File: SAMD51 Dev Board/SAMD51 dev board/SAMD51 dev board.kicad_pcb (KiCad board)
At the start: 4 copper layers, 98.9 x 130 mm, 56 parts, among them IC1 MCP1603-330I_MC, IC2 MCP1603-180I_MC, J1 Conn_02x08_Top_Bottom, J10 Conn_02x16_Top_Bottom, J11 Conn_01x07, J12 Conn_01x05, J13 Conn_01x08, J14 Conn_02x16_Top_Bottom, J15 Conn_01x05, J16 Conn_01x06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

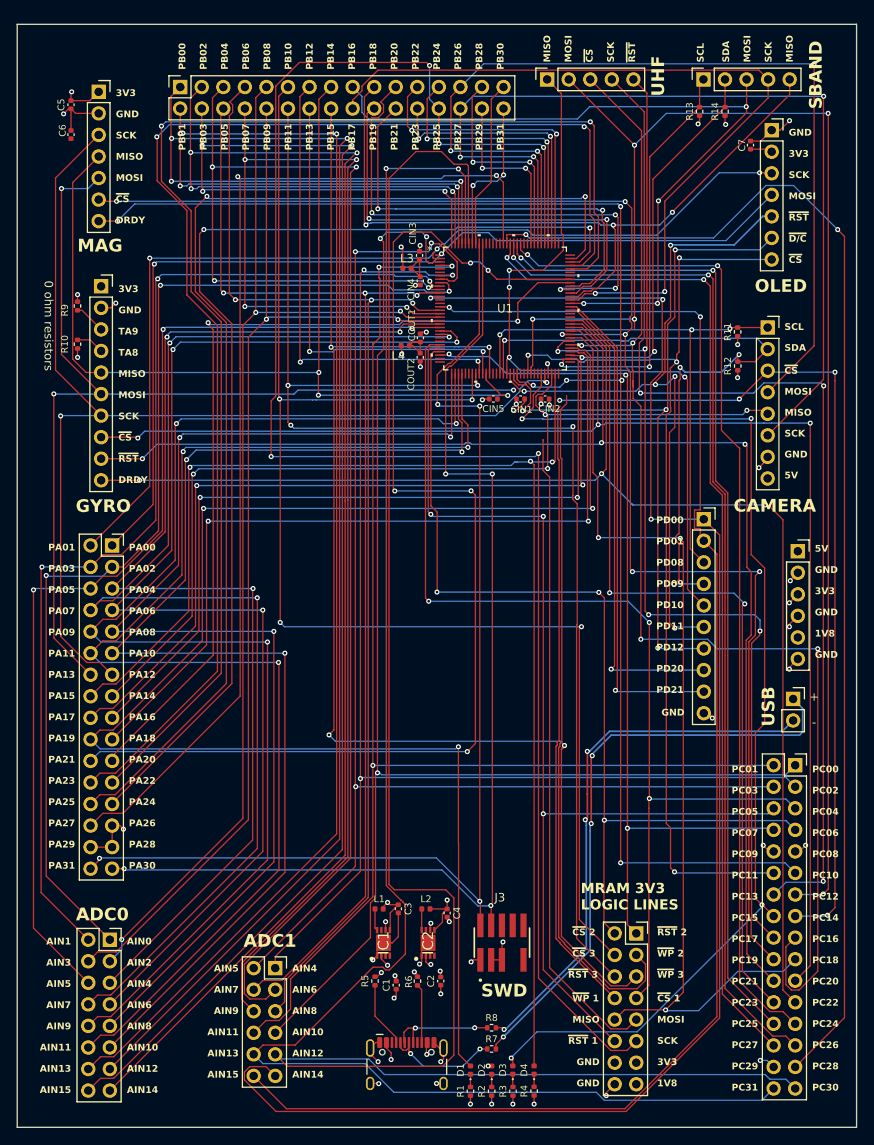
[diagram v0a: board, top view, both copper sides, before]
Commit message: routed samd51 breakout
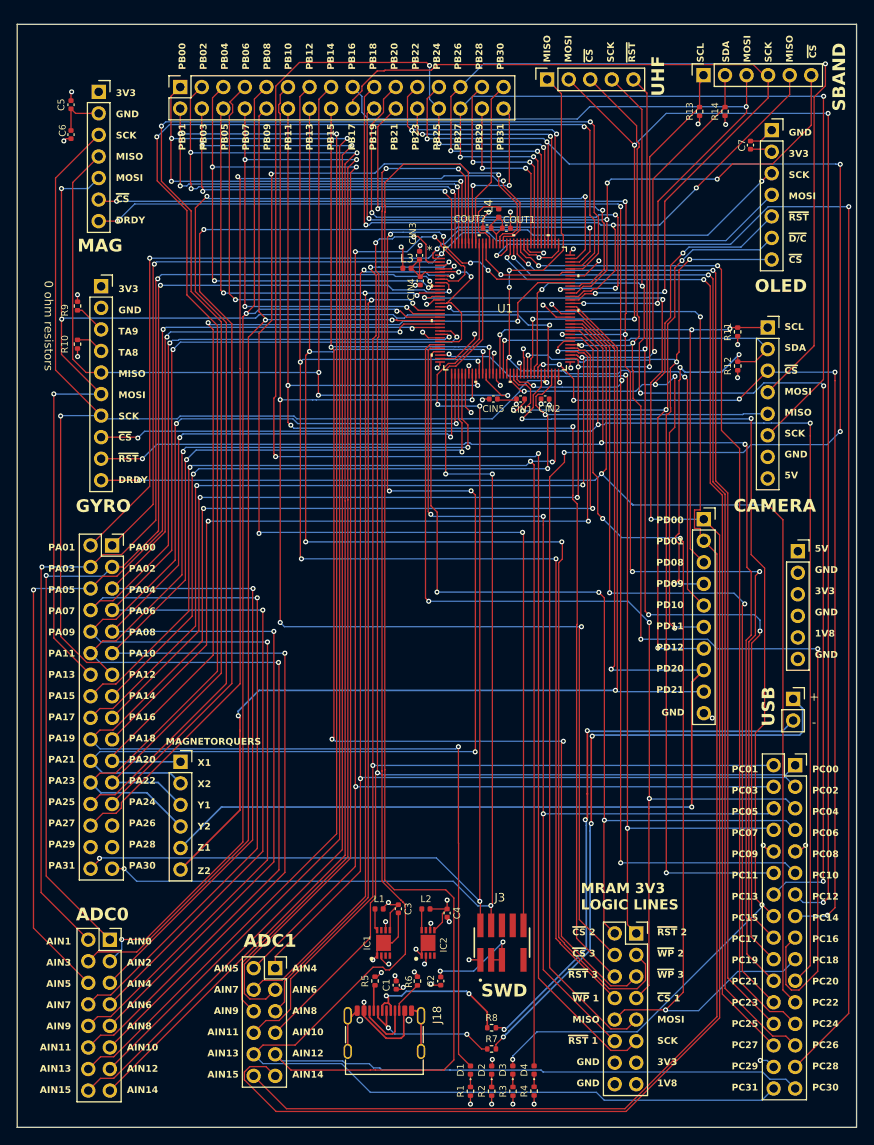
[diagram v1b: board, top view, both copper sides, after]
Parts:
- removed J2: USB_C_Receptacle_USB2.0_14P, Connector_USB:USB_C_Receptacle_HCTL_HC-TYPE-C-16P-01A
- added J18: USB_C_Receptacle_USB2.0_14P, Connector_USB:USB_C_Receptacle_G-Switch_GT-USB-7010ASV, F.Cu at (145.9, 148.2)
- added J19: Conn_01x06, Connector_PinSocket_2.54mm:PinSocket_1x06_P2.54mm_Vertical, F.Cu at (121.8, 115.2)
- J15: value Conn_01x05 -> Conn_01x06; footprint Connector_PinSocket_2.54mm:PinSocket_1x05_P2.54mm_Vertical -> Connector_PinSocket_2.54mm:PinSocket_1x06_P2.54mm_Vertical
- moved L4 19.1 mm to (159.3, 50.5), turned to 90 degrees
- moved COUT2 17.1 mm to (158.0, 52.3), turned to 180 degrees
- moved COUT1 16.4 mm to (160.2, 52.3), turned to 0 degrees
- moved J15 0.50 mm to (183.5, 34.2)
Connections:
- net PA20 renamed MTQ_X_IN1
- net PA21 renamed MTQ_X_IN2
- net PA22 renamed MTQ_Y_IN1
- net PA23 renamed MTQ_Y_IN2
- net PD20 renamed MTQ_Z_IN1
- net PD21 renamed MTQ_Z_IN2
- CIN3 pad 1: Net-(U1A-VDANA) -> Net-(CIN3-Pad1)
- CIN4 pad 1: Net-(U1A-VDANA) -> Net-(CIN3-Pad1)
- J10 pad 20: PB19 -> SBAND ~{CS}
- L3 pad 2: Net-(U1A-VDANA) -> Net-(CIN3-Pad1)
- U1 pad 106: (no net) -> GND
- U1 pad 107: (no net) -> +3V3
- U1 pad 114: (no net) -> SWD ~{RESET}
- U1 pad 115: (no net) -> Net-(U1A-VDDCORE)
- U1 pad 117: (no net) -> Net-(U1A-VSW)
- U1 pad 118: (no net) -> +3V3
- U1 pad 14: (no net) -> GND
- U1 pad 15: (no net) -> Net-(CIN3-Pad1)
- U1 pad 25: (no net) -> GND
- U1 pad 26: (no net) -> Net-(CIN3-Pad1)
- U1 pad 31: (no net) -> GND
- U1 pad 32: (no net) -> +3V3
- U1 pad 37: (no net) -> +3V3
- U1 pad 38: (no net) -> GND
- U1 pad 45: (no net) -> GND
- U1 pad 46: (no net) -> +3V3
- U1 pad 5: (no net) -> GND
- U1 pad 53: (no net) -> GND
- U1 pad 54: (no net) -> +3V3
- U1 pad 6: (no net) -> Net-(CIN3-Pad1)
- U1 pad 64: (no net) -> GND
- U1 pad 65: (no net) -> +3V3
- U1 pad 78: (no net) -> GND
- U1 pad 79: (no net) -> +3V3
- U1 pad 85: PB19 -> SBAND ~{CS}
- U1 pad 90: (no net) -> GND
- U1 pad 91: (no net) -> +3V3
- U1 pad 96: (no net) -> GND
- U1 pad 97: (no net) -> +3V3
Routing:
- net SWD ~{RESET}: track 0.00 -> 158.8 mm, vias 0 -> 4
- net MRAM MOSI: track 109.1 -> 208.7 mm, vias 2 -> 5
- net SBAND ~{CS}: track 0.00 -> 90.2 mm, vias 0 -> 4
- net MTQ_Z_IN1: track 56.2 -> 135.2 mm, vias 1 -> 2
- net MTQ_Z_IN2: track 58.5 -> 125.6 mm, vias 1 -> 2
- net PB19: track 53.1 -> 0.00 mm, vias 2 -> 0
- net +5V: track 154.8 -> 193.3 mm, vias 12 -> 11
- net MRAM 2 ~{WP}: track 133.0 -> 168.3 mm, vias 2 -> 4
- net MRAM 1 ~{WP}: track 128.5 -> 163.5 mm, vias 2 -> 4
- net Net-(CIN3-Pad1): track 0.00 -> 24.6 mm, vias 0 -> 2
- net GND: track 73.2 -> 96.4 mm, vias 36 -> 35
- net UHF SCK: track 126.0 -> 148.4 mm, vias 3 -> 5
- net MTQ_X_IN2: track 138.2 -> 152.7 mm, vias 5 -> 7
- net MAG/GYRO MOSI: track 121.6 -> 136.0 mm
- net MTQ_Y_IN2: track 156.3 -> 169.0 mm
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- removed copper zone on In2.Cu, net +5V
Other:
- board text added: "MAGNETORQUERS"
- board text added: "X1"
- board text added: "X2"
- board text added: "Y1"
- board text added: "Y2"
- board text added: "Z1"
- board text added: "Z2"
